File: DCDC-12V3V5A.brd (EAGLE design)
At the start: 40 x 24 mm, 37 parts, among them Q10 NMOSFET, Q9 NMOSFET, U1 LM3150MHX/NOPB

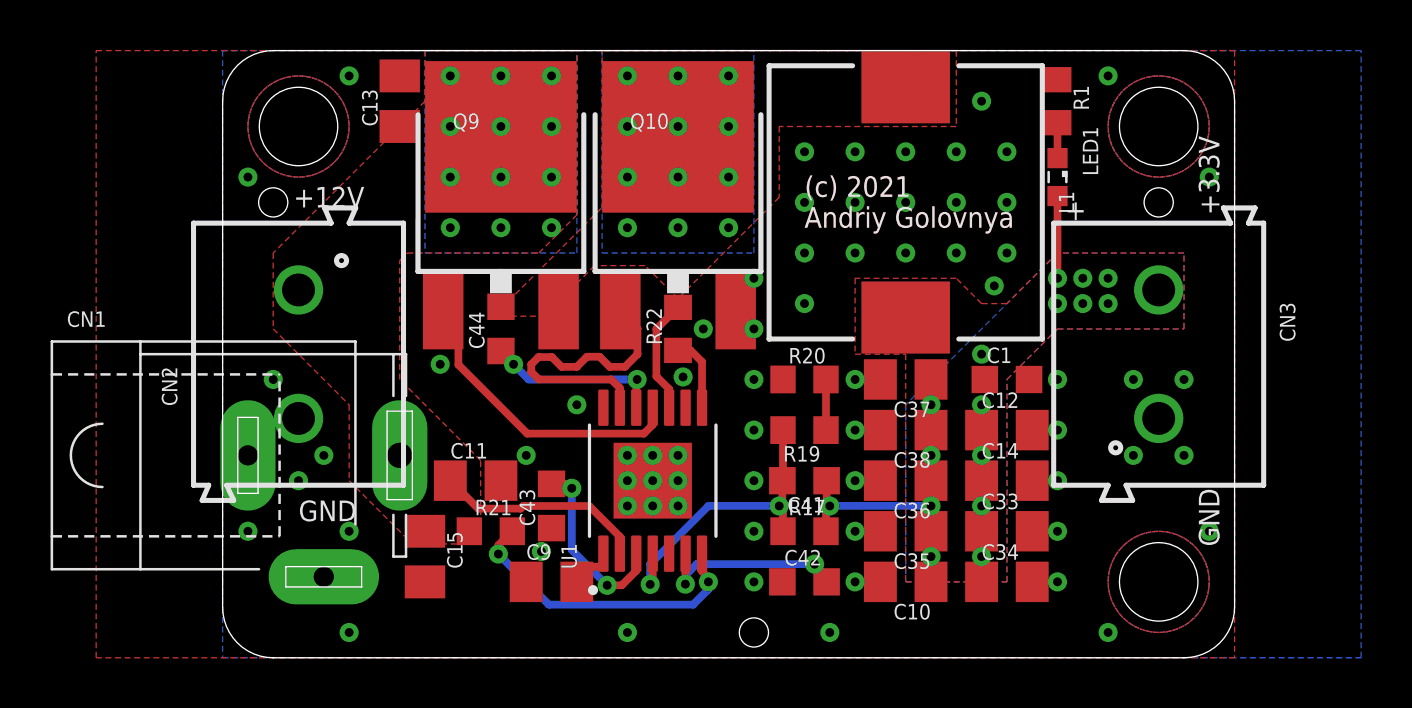
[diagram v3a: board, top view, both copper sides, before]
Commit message: Moved some texts and tooling holes a bit. Generated CAM files. Generated PNG preview. Generated PDF schematics. Renamed BoM and PnP files.
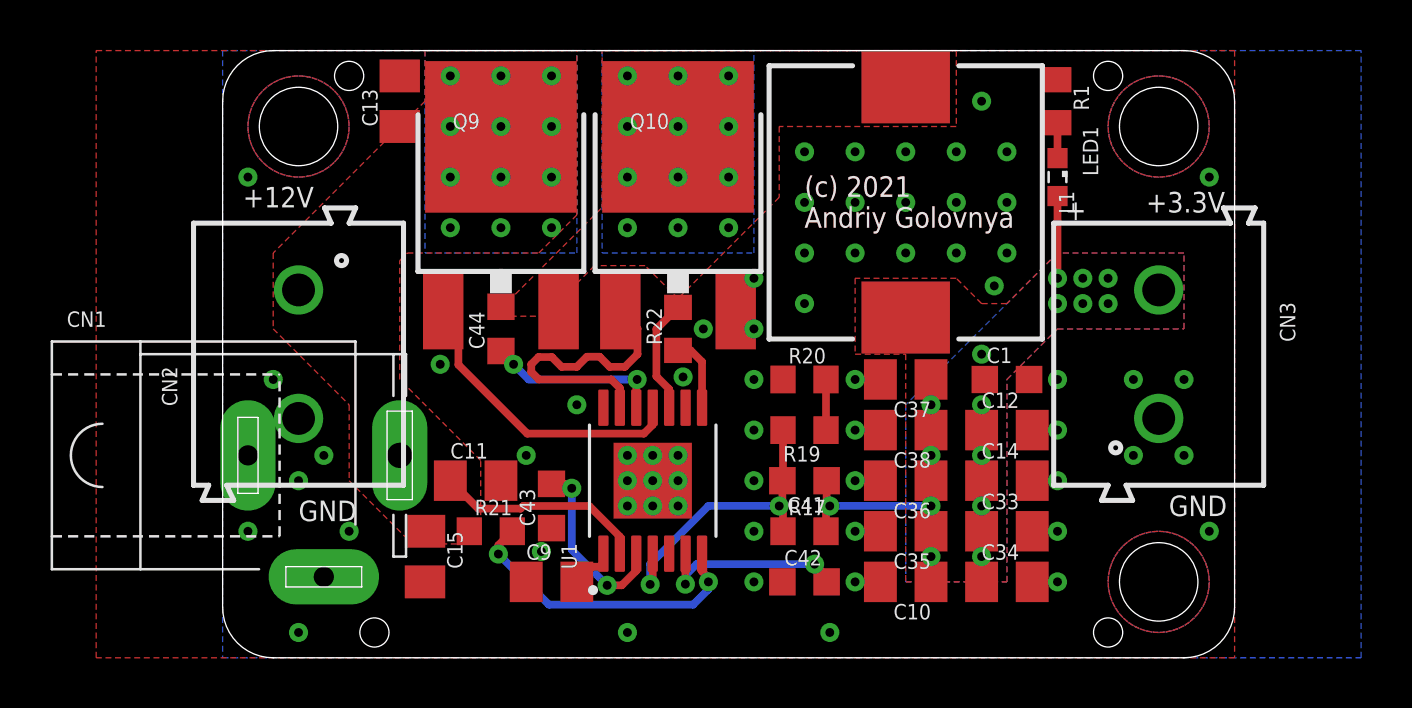
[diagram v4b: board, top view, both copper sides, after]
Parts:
- added HOLE4: TOOLINGHOLE, _my_fiducia:TOOLING-HOLE
- moved HOLE3 15.0 mm to (6.00, 1.00)
- moved HOLE2 5.83 mm to (5.00, 23.0)
- moved HOLE1 5.39 mm to (35.0, 23.0)
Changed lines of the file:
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@@
 <drawing>
 <settings>
-<setting alwaysvectorfont="no"/>
+<setting alwaysvectorfont="yes"/>
 <setting verticaltext="up"/>
 </settings>
@@
 <hole x="37" y="3" drill="3.1"/>
 <text x="33" y="20" size="1.6764" layer="22" font="vector" ratio="20" rot="MR0">DCDC-12V3V5A-0011</text>
-<text x="2.8" y="17.8" size="0.8128" layer="21" font="vector">+12V</text>
+<text x="0.8" y="17.8" size="0.8128" layer="21" font="vector">+12V</text>
 <text x="3" y="5.4" size="0.8128" layer="21" font="vector">GND</text>
-<text x="39.4" y="4.4" size="0.8128" layer="21" font="vector" rot="R90">GND</text>
-<text x="39.4" y="17.5" size="0.8128" layer="21" font="vector" rot="R90">+3.3V</text>
+<text x="37.4" y="5.6" size="0.8128" layer="21" font="vector">GND</text>
+<text x="36.5" y="17.6" size="0.8128" layer="21" font="vector">+3.3V</text>
 <text x="33" y="16" size="1.27" layer="22" font="vector" rot="MR0">(c) Andriy Golovnya</text>
 <text x="33" y="18" size="1.27" layer="22" font="vector" rot="MR0">3.3V/5A DC-DC Buck Converter</text>
@@
 <attribute name="VALUE" x="31.095" y="22.635" size="0.6096" layer="27" font="vector" rot="R270"/>
 </element>
-<element name="HOLE1" library="_my_fiducia" package="TOOLING-HOLE" value="TOOLINGHOLE" x="37" y="18" smashed="yes"/>
-<element name="HOLE2" library="_my_fiducia" package="TOOLING-HOLE" value="TOOLINGHOLE" x="2" y="18" smashed="yes"/>
-<element name="HOLE3" library="_my_fiducia" package="TOOLING-HOLE" value="TOOLINGHOLE" x="21" y="1" smashed="yes"/>
+<element name="HOLE1" library="_my_fiducia" package="TOOLING-HOLE" value="TOOLINGHOLE" x="35" y="23" smashed="yes"/>
+<element name="HOLE2" library="_my_fiducia" package="TOOLING-HOLE" value="TOOLINGHOLE" x="5" y="23" smashed="yes"/>
+<element name="HOLE3" library="_my_fiducia" package="TOOLING-HOLE" value="TOOLINGHOLE" x="6" y="1" smashed="yes"/>
 <element name="C1" library="rcl" library_urn="urn:adsk.eagle:library:334" package="C0603K" package3d_urn="urn:adsk.eagle:package:23680/2" value="1nF" x="31" y="11" smashed="yes">
 <attribute name="NAME" x="30.2" y="11.65" size="0.6096" layer="25" font="vector"/>
@@
 <attribute name="VALUE" x="30.2" y="9.35" size="0.6096" layer="27" font="vector"/>
 </element>
+<element name="HOLE4" library="_my_fiducia" package="TOOLING-HOLE" value="TOOLINGHOLE" x="35" y="1" smashed="yes"/>
 </elements>
 <signals>
@@
 <via x="33" y="5" extent="1-16" drill="0.35"/>
 <via x="33" y="3" extent="1-16" drill="0.35"/>
-<via x="5" y="23" extent="1-16" drill="0.35"/>
 <via x="30.5" y="14.7" extent="1-16" drill="0.35"/>
 <via x="30" y="22" extent="1-16" drill="0.35"/>
-<via x="35" y="23" extent="1-16" drill="0.35"/>
 <via x="39" y="19" extent="1-16" drill="0.35"/>
 <via x="39" y="5" extent="1-16" drill="0.35"/>
@@
 <via x="1" y="5" extent="1-16" drill="0.35"/>
 <via x="1" y="19" extent="1-16" drill="0.35"/>
-<via x="35" y="1" extent="1-16" drill="0.35"/>
 <via x="17" y="8" extent="1-16" drill="0.35"/>
 <via x="17" y="7" extent="1-16" drill="0.35"/>
@@
 <via x="4" y="8" extent="1-16" drill="0.35"/>
 <via x="2" y="11" extent="1-16" drill="0.35"/>
-<via x="5" y="1" extent="1-16" drill="0.35"/>
+<via x="3" y="1" extent="1-16" drill="0.35"/>
 <via x="12" y="8" extent="1-16" drill="0.35"/>
 <via x="12.6" y="4.2" extent="1-16" drill="0.35"/>
@@
 <via x="30" y="12" extent="1-16" drill="0.35"/>
 <wire x1="33" y1="18.25" x2="33" y2="15" width="0.3048" layer="1"/>
-<wire x1="35" y1="15" x2="37" y2="14.54" width="0" layer="19" extent="1-1"/>
-<wire x1="35" y1="14" x2="35" y2="15" width="0" layer="19" extent="1-1"/>
-<wire x1="34" y1="15" x2="35" y2="15" width="0" layer="19" extent="1-1"/>
-<wire x1="34" y1="14" x2="35" y2="14" width="0" layer="19" extent="1-1"/>
-<wire x1="33" y1="14" x2="34" y2="14" width="0" layer="19" extent="1-1"/>
-<wire x1="33" y1="15" x2="34" y2="15" width="0" layer="19" extent="1-1"/>
-<wire x1="30" y1="12" x2="33" y2="14" width="0" layer="19" extent="1-1"/>
-<wire x1="30.125" y1="11" x2="30" y2="12" width="0" layer="19" extent="1-1"/>
-<wire x1="30" y1="10" x2="30.125" y2="11" width="0" layer="19" extent="1-1"/>
-<wire x1="30" y1="9" x2="30" y2="10" width="0" layer="19" extent="1-1"/>
-<wire x1="30" y1="8" x2="30" y2="9" width="0" layer="19" extent="1-1"/>
-<wire x1="30" y1="7" x2="30" y2="8" width="0" layer="19" extent="1-1"/>
-<wire x1="30" y1="6" x2="30" y2="7" width="0" layer="19" extent="1-1"/>
-<wire x1="30" y1="5" x2="30" y2="6" width="0" layer="19" extent="1-1"/>
-<wire x1="30" y1="4" x2="30" y2="5" width="0" layer="19" extent="1-1"/>
-<wire x1="30" y1="3" x2="30" y2="4" width="0" layer="19" extent="1-1"/>
-<wire x1="28" y1="9" x2="30" y2="9" width="0" layer="19" extent="1-1"/>
-<wire x1="28" y1="10" x2="28" y2="9" width="0" layer="19" extent="1-1"/>
-<wire x1="28" y1="11" x2="28" y2="10" width="0" layer="19" extent="1-1"/>
-<wire x1="28" y1="8" x2="28" y2="9" width="0" layer="19" extent="1-1"/>
-<wire x1="28" y1="7" x2="28" y2="8" width="0" layer="19" extent="1-1"/>
-<wire x1="28" y1="6" x2="28" y2="7" width="0" layer="19" extent="1-1"/>
-<wire x1="28" y1="5" x2="28" y2="6" width="0" layer="19" extent="1-1"/>
-<wire x1="28" y1="4" x2="28" y2="5" width="0" layer="19" extent="1-1"/>
-<wire x1="28" y1="3" x2="28" y2="4" width="0" layer="19" extent="1-1"/>
-<wire x1="27" y1="13.45" x2="28" y2="11" width="0" layer="19" extent="1-1"/>
 </signal>
 <signal name="BUCK_LG">

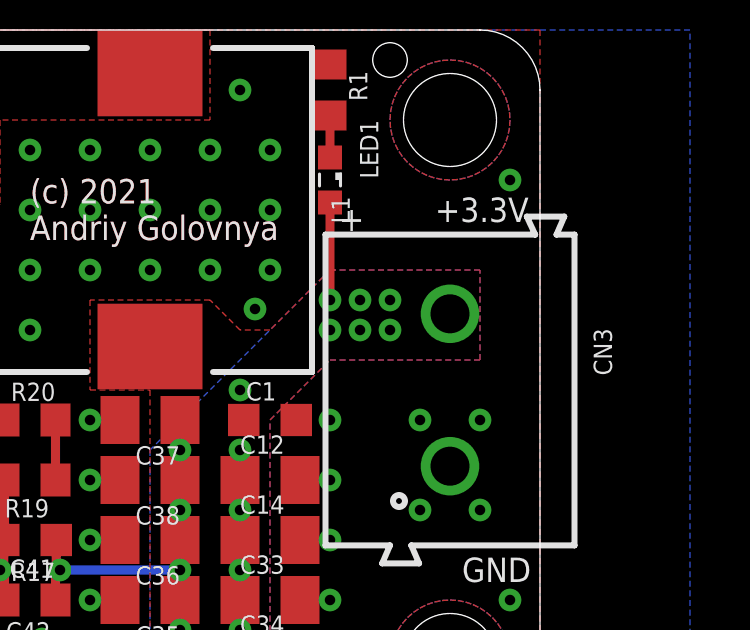
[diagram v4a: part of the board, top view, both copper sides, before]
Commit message: Added few vias. Generated CAM files. Generated PNG preview. Renamed BoM and PnP files.
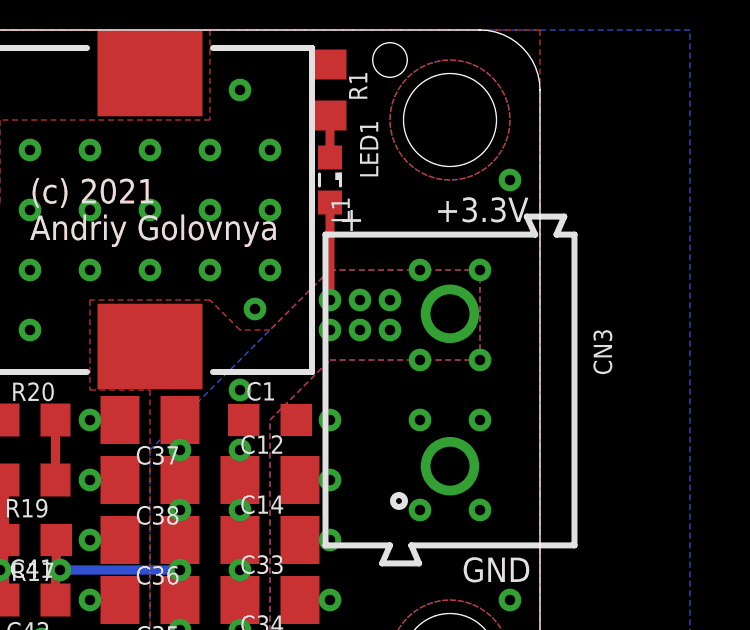
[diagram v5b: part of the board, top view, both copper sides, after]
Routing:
- net 3.3V: vias 16 -> 20
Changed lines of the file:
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@@
 <drawing>
 <settings>
-<setting alwaysvectorfont="yes"/>
+<setting alwaysvectorfont="no"/>
 <setting verticaltext="up"/>
 </settings>
@@
 <via x="30" y="12" extent="1-16" drill="0.35"/>
 <wire x1="33" y1="18.25" x2="33" y2="15" width="0.3048" layer="1"/>
+<via x="38" y="16" extent="1-16" drill="0.35"/>
+<via x="36" y="16" extent="1-16" drill="0.35"/>
+<via x="36" y="13" extent="1-16" drill="0.35"/>
+<via x="38" y="13" extent="1-16" drill="0.35"/>
 </signal>
 <signal name="BUCK_LG">
